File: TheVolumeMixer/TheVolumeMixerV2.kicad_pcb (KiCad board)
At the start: 2 copper layers, 75 x 59 mm, 58 parts, among them J1 Conn_01x01_Male, J10 Conn_01x01_Male, J2 Conn_01x01_Male, J3 Conn_01x05, J4 Conn_01x01_Male, J5 Conn_01x01_Male, J6 Conn_01x01_Male, J7 Conn_01x01_Male, J8 SJ1-3544, J9 Conn_01x01_Male, U1 TLC5947RHB, U2 ATSAMD21G18A-A, U3 AP2127K-3.3, U4 TPA2017, Y1 32.768kHz

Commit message: updated Notes and made PCB updates
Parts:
- moved C8 17.1 mm to (145.0, 86.0), turned to 180 degrees
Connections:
- U2 pad 13: /VOL3 -> /VOL4
- U2 pad 15: /VOL4 -> /VOL3
- U2 pad 16: /SP_GC1 -> Net-(U2-Pad16)
- U2 pad 30: Net-(U2-Pad30) -> /SP_GC1
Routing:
- net +3V3: track 106.6 -> 101.1 mm
- net /VOL3: track 28.1 -> 30.5 mm
- net /VOL4: track 45.3 -> 43.5 mm

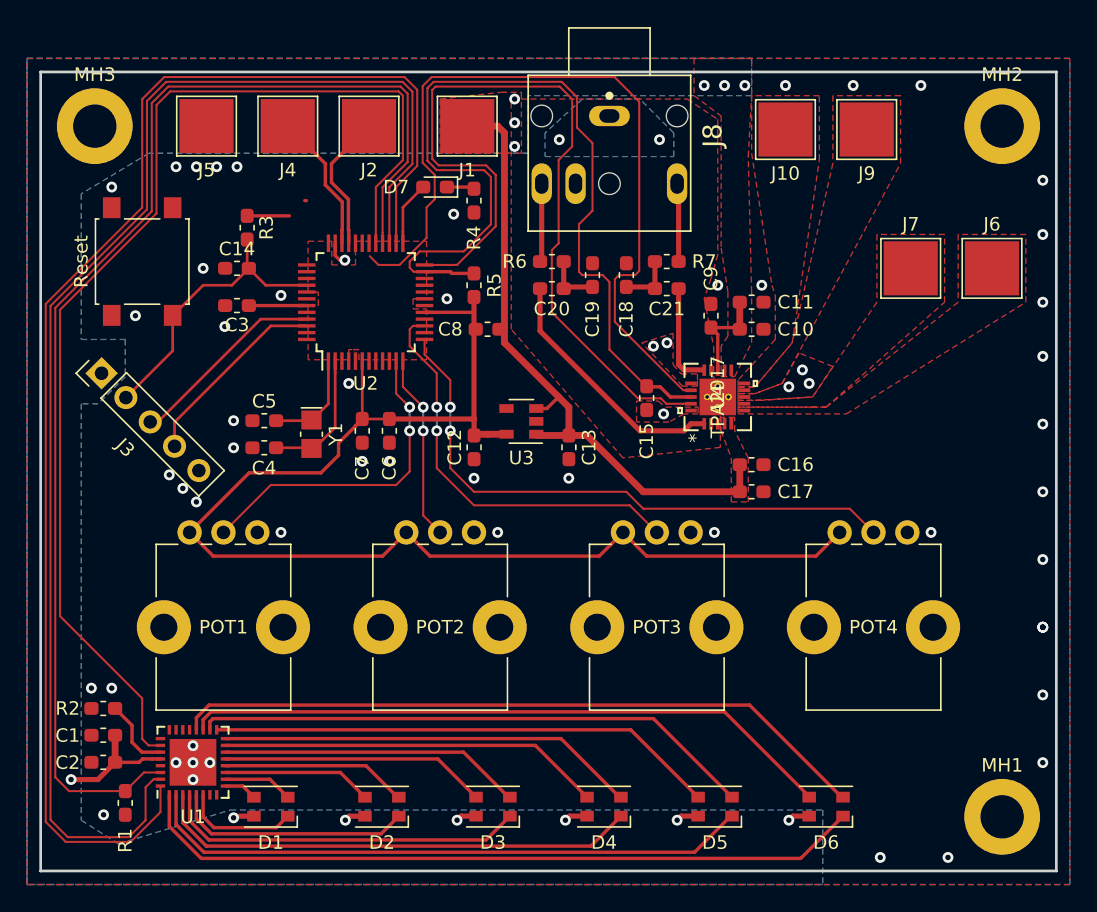
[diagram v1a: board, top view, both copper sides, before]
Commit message: PCB finished, Gerbers exported
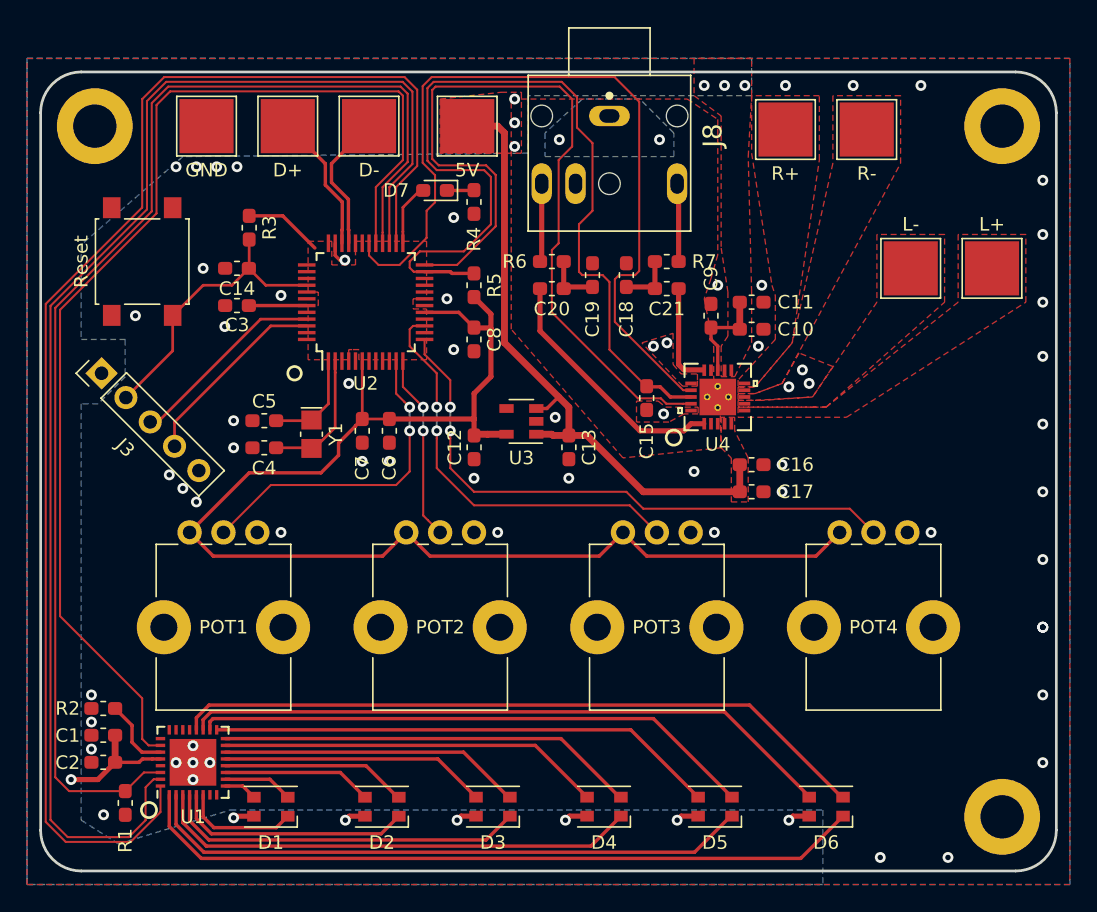
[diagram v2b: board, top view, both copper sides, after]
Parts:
- U4: value TPA2017 -> (none)
- moved C8 1.25 mm to (144.0, 86.8), turned to 90 degrees
- moved D7 0.25 mm to (141.1, 75.8)
- moved R3 0.15 mm to (127.4, 78.5)
- moved R4 0.10 mm to (144.0, 76.6)
- renumbered J1 to 5V, J4 to D+, J2 to D-, J5 to GND, J6 to L+, J7 to L-, J10 to R+, J9 to R-
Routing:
- net +3V3: track 101.1 -> 106.7 mm
- net /SP_GC1: track 59.6 -> 60.5 mm
- net GND: track 1.88 -> 1.76 mm, vias 59 -> 65
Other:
- outline, holes or cut-outs redrawn

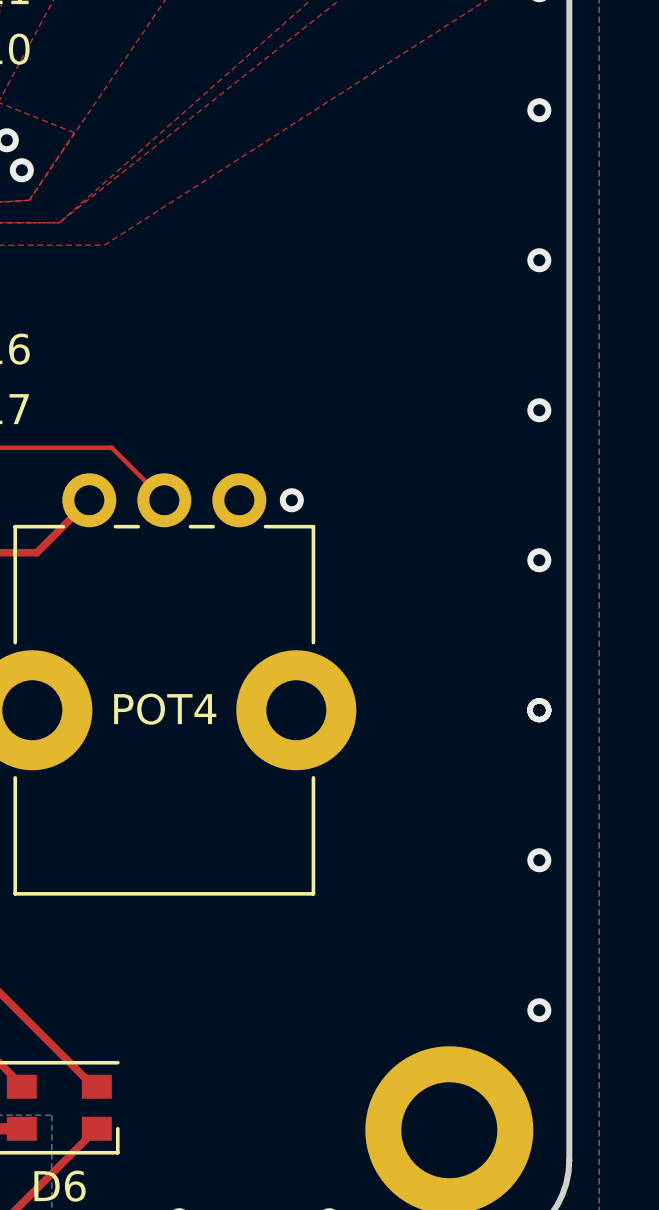
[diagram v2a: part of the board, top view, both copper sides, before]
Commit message: made changes to SilkScreen. Regened Gerbers
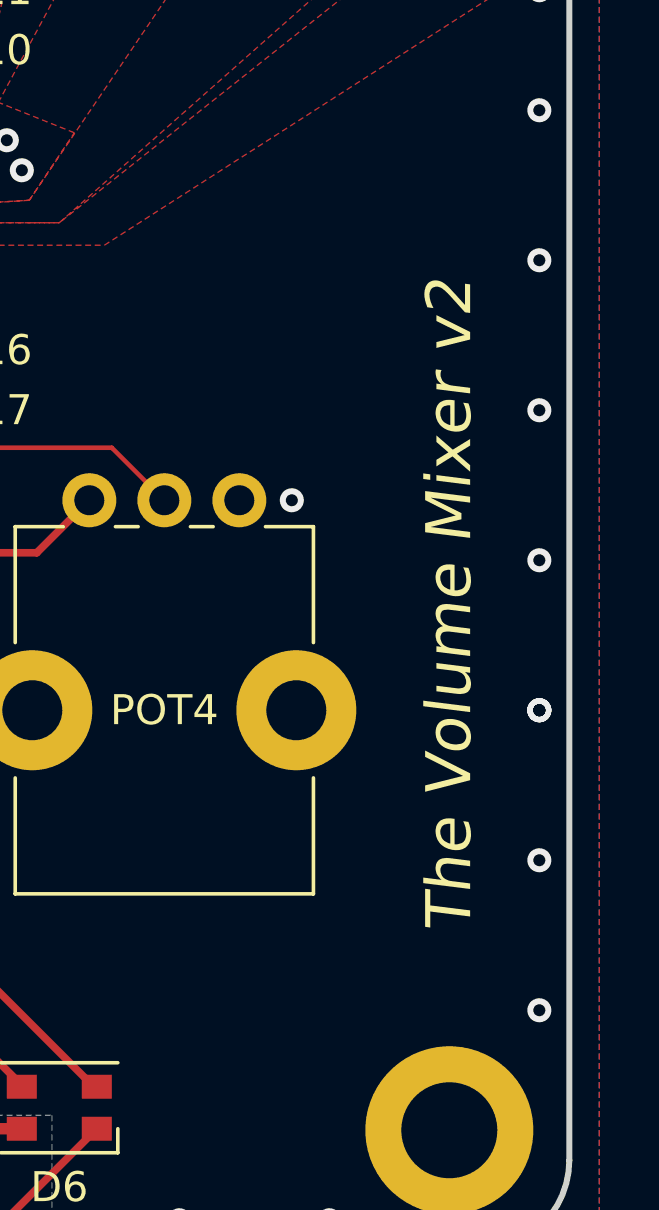
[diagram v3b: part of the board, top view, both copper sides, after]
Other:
- board text added: "POT1"
- board text added: "POT2"
- board text added: "POT3"
- board text added: "POT4"
- board text added: "The Volume Mixer v2"
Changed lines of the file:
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@@
   (general
     (thickness 1.6)
-    (drawings 11)
+    (drawings 16)
     (tracks 465)
     (zones 0)
@@
     (34 B.Paste user hide)
     (35 F.Paste user)
-    (36 B.SilkS user hide)
+    (36 B.SilkS user)
     (37 F.SilkS user)
     (38 B.Mask user)
@@
     )
   )
+  (gr_text "The Volume Mixer v2" (at 183 104.5 90) (layer F.SilkS)
+    (effects (font (size 1.5 1.5) (thickness 0.3) italic))
+  )
+  (gr_text POT4 (at 173.5 108) (layer B.SilkS)
+    (effects (font (size 1 1) (thickness 0.15)) (justify mirror))
+  )
+  (gr_text POT3 (at 157.5 108) (layer B.SilkS)
+    (effects (font (size 1 1) (thickness 0.15)) (justify mirror))
+  )
+  (gr_text POT2 (at 141.5 108) (layer B.SilkS)
+    (effects (font (size 1 1) (thickness 0.15)) (justify mirror))
+  )
+  (gr_text POT1 (at 125.5 108) (layer B.SilkS)
+    (effects (font (size 1 1) (thickness 0.15)) (justify mirror))
+  )
   (gr_circle (center 120 121.5) (end 120.25 121) (layer F.SilkS) (width 0.2))
